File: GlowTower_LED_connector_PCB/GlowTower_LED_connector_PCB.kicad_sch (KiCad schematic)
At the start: 4 parts, among them U1 LED strip, U2 LED strip, U3 LED strip, U4 LED strip

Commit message: updated pcb design (in progress)
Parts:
- removed U1, U2, U3, U4: LED strip, Connector:LED strip connector pad, symbol Connector:LED_strip_contact_pads
- added SW1: TS-1102S-C-A-B, TS-1102S-C-A-B:TS-1102S-C-A-B, symbol TS-1102S-C-A-B:TS-1102S-C-A-B
- added U1, U2, U3, U4: (no value), symbol myparts:LED_strip_contact_4pads
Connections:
- new net: U1.3 (GND), U3.2 (Data)
- new net: U2.3 (GND), U4.2 (Data)
- new net BUTTON: SW1.1, U1.1 (5V)
- new net GND: SW1.3, U1.2 (Data)
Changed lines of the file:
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@@
 (kicad_sch (version 20211123) (generator eeschema)
   (paper "A5")
-  (wire (pts (xy 90.17 62.23) (xy 118.11 62.23))
+  (wire (pts (xy 90.17 64.77) (xy 105.41 64.77))
     (stroke (width 0) (type default) (color 0 0 0 0))
   )
-  (wire (pts (xy 90.17 77.47) (xy 118.11 77.47))
+  (wire (pts (xy 105.41 78.74) (xy 105.41 80.01))
+    (stroke (width 0) (type default) (color 0 0 0 0))
+  )
+  (wire (pts (xy 90.17 59.69) (xy 95.25 59.69))
+    (stroke (width 0) (type default) (color 0 0 0 0))
+  )
+  (wire (pts (xy 33.02 102.87) (xy 38.1 102.87))
+    (stroke (width 0) (type default) (color 0 0 0 0))
+  )
+  (wire (pts (xy 90.17 62.23) (xy 95.25 62.23))
+    (stroke (width 0) (type default) (color 0 0 0 0))
+  )
+  (wire (pts (xy 34.29 113.03) (xy 38.1 113.03))
+    (stroke (width 0) (type default) (color 0 0 0 0))
+  )
+  (wire (pts (xy 105.41 63.5) (xy 120.65 63.5))
+    (stroke (width 0) (type default) (color 0 0 0 0))
+  )
+  (wire (pts (xy 105.41 80.01) (xy 90.17 80.01))
+    (stroke (width 0) (type default) (color 0 0 0 0))
+  )
+  (wire (pts (xy 105.41 64.77) (xy 105.41 63.5))
+    (stroke (width 0) (type default) (color 0 0 0 0))
+  )
+  (wire (pts (xy 105.41 78.74) (xy 120.65 78.74))
     (stroke (width 0) (type default) (color 0 0 0 0))
   )
@@
     (effects (font (size 3 3)) (justify left bottom))
   )
-  (symbol (lib_name "LED_strip_contact_pads_7") (lib_id "Connector:LED_strip_contact_pads") (at 121.92 80.01 0) (mirror x) (unit 1)
-    (in_bom yes) (on_board yes)
-    (property "Reference" "U4" (id 0) (at 127 76.2 0)
-      (effects (font (size 1.27 1.27)) (justify left))
+  (global_label "BUTTON" (shape input) (at 95.25 59.69 0) (fields_autoplaced)
+    (effects (font (size 1.27 1.27)) (justify left))
+    (property "Intersheet References" "${INTERSHEET_REFS}" (id 0) (at 104.8598 59.6106 0)
+      (effects (font (size 1.27 1.27)) (justify left) hide)
     )
-    (property "Value" "LED strip" (id 1) (at 127 78.74 0)
-      (effects (font (size 1.27 1.27)) (justify left))
+  )
+  (global_label "BUTTON" (shape input) (at 33.02 102.87 180) (fields_autoplaced)
+    (effects (font (size 1.27 1.27)) (justify right))
+    (property "Intersheet References" "${INTERSHEET_REFS}" (id 0) (at 23.4102 102.9494 0)
+      (effects (font (size 1.27 1.27)) (justify right) hide)
     )
-    (property "Footprint" "Connector:LED strip connector pad" (id 2) (at 121.92 80.01 0)
+  )
+  (symbol (lib_id "power:GND") (at 95.25 62.23 90) (unit 1)
+    (in_bom yes) (on_board yes) (fields_autoplaced)
+    (property "Reference" "#PWR0101" (id 0) (at 101.6 62.23 0)
       (effects (font (size 1.27 1.27)) hide)
     )
-    (property "Datasheet" "" (id 3) (at 121.92 80.01 0)
+    (property "Value" "GND" (id 1) (at 99.06 62.2301 90)
+      (effects (font (size 1.27 1.27)) (justify right))
+    )
+    (property "Footprint" "" (id 2) (at 95.25 62.23 0)
       (effects (font (size 1.27 1.27)) hide)
+    )
+    (property "Datasheet" "" (id 3) (at 95.25 62.23 0)
+      (effects (font (size 1.27 1.27)) hide)
+    )
+    (pin "1")
+  )
+  (symbol (lib_id "TS-1102S-C-A-B:TS-1102S-C-A-B") (at 25.4 107.95 0) (unit 1)
+    (in_bom yes) (on_board yes) (fields_autoplaced)
+    (property "Reference" "SW1" (id 0) (at 50.8 97.79 0))
+    (property "Value" "TS-1102S-C-A-B" (id 1) (at 50.8 100.33 0))
+    (property "Footprint" "TS-1102S-C-A-B:TS-1102S-C-A-B" (id 2) (at 25.4 118.11 0)
+      (effects (font (size 1.27 1.27) italic) hide)
+    )
+    (property "Datasheet" "https://datasheet.lcsc.com/lcsc/2110151630_XKB-Connectivity-TS-1102S-C-A-B_C381038.pdf" (id 3) (at 23.114 107.823 0)
+      (effects (font (size 1.27 1.27)) (justify left) hide)
     )
     (pin "1")
     (pin "2")
     (pin "3")
+    (pin "4")
   )
-  (symbol (lib_name "LED_strip_contact_pads_6") (lib_id "Connector:LED_strip_contact_pads") (at 121.92 64.77 0) (mirror x) (unit 1)
+  (symbol (lib_id "myparts:LED_strip_contact_4pads") (at 86.36 59.69 0) (mirror y) (unit 1)
     (in_bom yes) (on_board yes)
-    (property "Reference" "U3" (id 0) (at 127 60.96 0)
+    (property "Reference" "U1" (id 0) (at 77.47 60.96 0)
       (effects (font (size 1.27 1.27)) (justify left))
     )
-    (property "Value" "LED strip" (id 1) (at 127 63.5 0)
+    (property "Value" "" (id 1) (at 77.47 63.5 0)
       (effects (font (size 1.27 1.27)) (justify left))
     )
-    (property "Footprint" "Connector:LED strip connector pad" (id 2) (at 121.92 64.77 0)
-      (effects (font (size 1.27 1.27)) hide)
-    )
-    (property "Datasheet" "" (id 3) (at 121.92 64.77 0)
-      (effects (font (size 1.27 1.27)) hide)
-    )
-    (pin "1")
-    (pin "2")
-    (pin "3")
-  )
-  (symbol (lib_name "LED_strip_contact_pads_3") (lib_id "Connector:LED_strip_contact_pads") (at 86.36 59.69 0) (mirror y) (unit 1)
-    (in_bom yes) (on_board yes)
-    (property "Reference" "U1" (id 0) (at 81.28 60.96 0)
-      (effects (font (size 1.27 1.27)) (justify left))
-    )
-    (property "Value" "LED strip" (id 1) (at 81.28 63.5 0)
-      (effects (font (size 1.27 1.27)) (justify left))
-    )
-    (property "Footprint" "Connector:LED strip connector pad" (id 2) (at 86.36 59.69 0)
+    (property "Footprint" "" (id 2) (at 86.36 59.69 0)
       (effects (font (size 1.27 1.27)) hide)
     )
@@
     (pin "2")
     (pin "3")
+    (pin "4")
   )
-  (symbol (lib_id "Connector:LED_strip_contact_pads") (at 86.36 74.93 0) (mirror y) (unit 1)
+  (symbol (lib_id "myparts:LED_strip_contact_4pads") (at 124.46 66.04 0) (mirror x) (unit 1)
     (in_bom yes) (on_board yes)
-    (property "Reference" "U2" (id 0) (at 78.74 74.93 0))
-    (property "Value" "LED strip" (id 1) (at 76.2 77.47 0))
-    (property "Footprint" "Connector:LED strip connector pad" (id 2) (at 86.36 74.93 0)
+    (property "Reference" "U3" (id 0) (at 134.62 60.96 0))
+    (property "Value" "" (id 1) (at 137.16 63.5 0))
+    (property "Footprint" "" (id 2) (at 124.46 66.04 0)
+      (effects (font (size 1.27 1.27)) hide)
+    )
+    (property "Datasheet" "" (id 3) (at 124.46 66.04 0)
+      (effects (font (size 1.27 1.27)) hide)
+    )
+    (pin "1")
+    (pin "2")
+    (pin "3")
+    (pin "4")
+  )
+  (symbol (lib_id "myparts:LED_strip_contact_4pads") (at 86.36 74.93 0) (mirror y) (unit 1)
+    (in_bom yes) (on_board yes)
+    (property "Reference" "U2" (id 0) (at 73.66 76.2 0))
+    (property "Value" "" (id 1) (at 73.66 78.74 0))
+    (property "Footprint" "" (id 2) (at 86.36 74.93 0)
       (effects (font (size 1.27 1.27)) hide)
     )
@@
     (pin "2")
     (pin "3")
+    (pin "4")
+  )
+  (symbol (lib_id "myparts:LED_strip_contact_4pads") (at 124.46 81.28 0) (mirror x) (unit 1)
+    (in_bom yes) (on_board yes)
+    (property "Reference" "U4" (id 0) (at 134.62 76.2 0))
+    (property "Value" "" (id 1) (at 137.16 78.74 0))
+    (property "Footprint" "" (id 2) (at 124.46 81.28 0)
+      (effects (font (size 1.27 1.27)) hide)
+    )
+    (property "Datasheet" "" (id 3) (at 124.46 81.28 0)
+      (effects (font (size 1.27 1.27)) hide)
+    )
+    (pin "1")
+    (pin "2")
+    (pin "3")
+    (pin "4")
+  )
+  (symbol (lib_id "power:GND") (at 34.29 113.03 270) (unit 1)
+    (in_bom yes) (on_board yes) (fields_autoplaced)
+    (property "Reference" "#PWR0102" (id 0) (at 27.94 113.03 0)
+      (effects (font (size 1.27 1.27)) hide)
+    )
+    (property "Value" "GND" (id 1) (at 30.48 113.0299 90)
+      (effects (font (size 1.27 1.27)) (justify right))
+    )
+    (property "Footprint" "" (id 2) (at 34.29 113.03 0)
+      (effects (font (size 1.27 1.27)) hide)
+    )
+    (property "Datasheet" "" (id 3) (at 34.29 113.03 0)
+      (effects (font (size 1.27 1.27)) hide)
+    )
+    (pin "1")
   )
   (sheet_instances
@@
   )
   (symbol_instances
-    (path "/ec5c2062-3a41-4636-8803-069e60a1641a"
-      (reference "U1") (unit 1) (value "LED strip") (footprint "Connector:LED strip connector pad")
+    (path "/21ef1968-a0fb-4b57-9c15-bd9b4521a1f0"
+      (reference "#PWR0101") (unit 1) (value "GND") (footprint "")
     )
-    (path "/f7667b23-296e-4362-a7e3-949632c8954b"
-      (reference "U2") (unit 1) (value "LED strip") (footprint "Connector:LED strip connector pad")
+    (path "/f102ecb1-5700-4820-807d-48fca6baaf4c"
+      (reference "#PWR0102") (unit 1) (value "GND") (footprint "")
     )
-    (path "/e4aa537c-eb9d-4dbb-ac87-fae46af42391"
-      (reference "U3") (unit 1) (value "LED strip") (footprint "Connector:LED strip connector pad")
+    (path "/3b3e6374-7870-4e9c-84dd-c6c9c8713fb1"
+      (reference "SW1") (unit 1) (value "TS-1102S-C-A-B") (footprint "TS-1102S-C-A-B:TS-1102S-C-A-B")
     )
-    (path "/9cbf35b8-f4d3-42a3-bb16-04ffd03fd8fd"
-      (reference "U4") (unit 1) (value "LED strip") (footprint "Connector:LED strip connector pad")
+    (path "/903d73dd-fd56-4103-90bf-a45d09a814bc"
+      (reference "U1") (unit 1) (value "LED strip") (footprint "myparts:LED strip connector 4pad supersmall")
+    )
+    (path "/b7b0b493-76e8-42d7-8e67-da2911f556ce"
+      (reference "U2") (unit 1) (value "LED strip") (footprint "myparts:LED strip connector 4pad supersmall")
+    )
+    (path "/a348a15e-9dd1-4384-9b04-af86a24d97fb"
+      (reference "U3") (unit 1) (value "LED strip") (footprint "myparts:LED strip connector 4pad supersmall")
+    )
+    (path "/d7a66b26-e013-45ce-92d1-9a5f78ecf5ef"
+      (reference "U4") (unit 1) (value "LED strip") (footprint "myparts:LED strip connector 4pad supersmall")
     )
   )

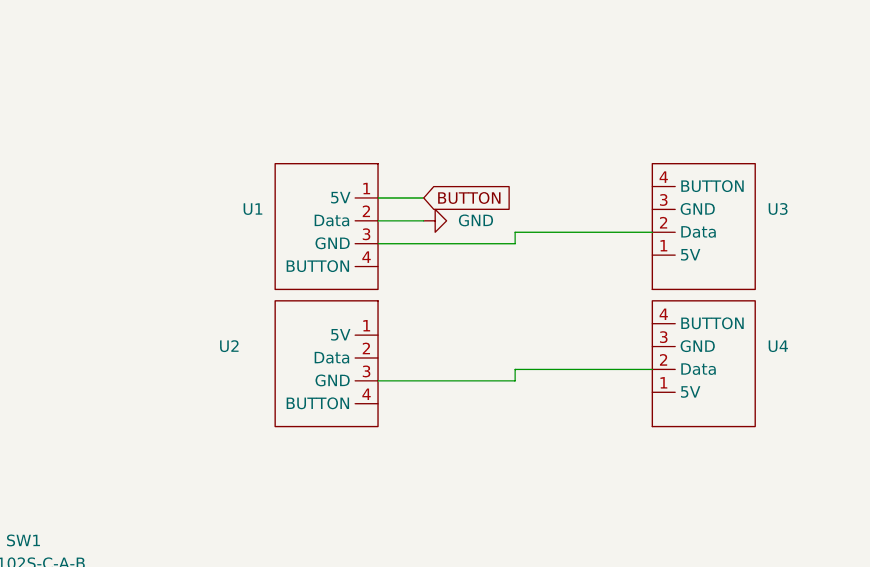
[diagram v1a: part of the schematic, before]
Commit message: redesigned GlowTower/GlowLight main pcb
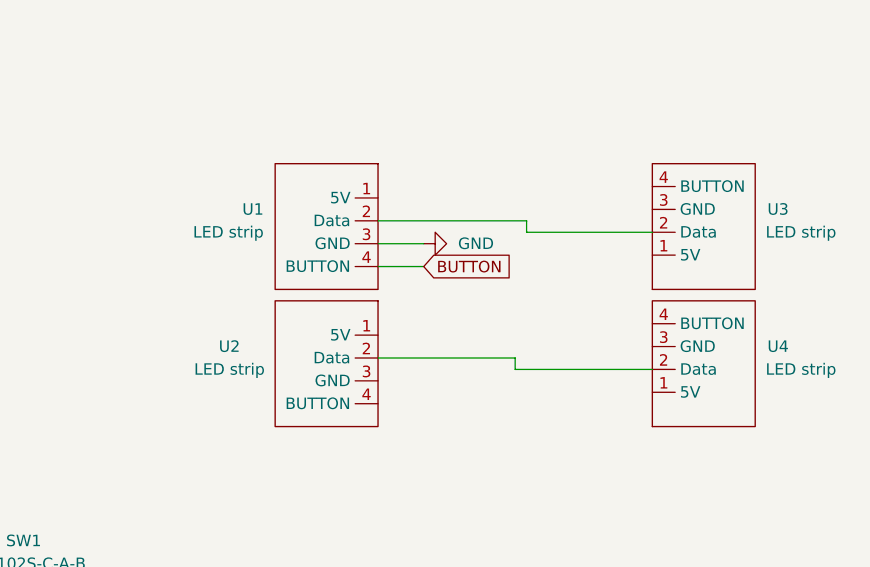
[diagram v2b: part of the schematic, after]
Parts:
- U1, U2, U3, U4: value (none) -> LED strip; footprint (none) -> myparts:LED strip connector 4pad
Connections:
- net BUTTON: now also U1.4 (BUTTON); no longer U1.1 (5V)
- net GND: now also U1.3 (GND); no longer U1.2 (Data)
- net at U3.2 (Data): now also U1.2 (Data); no longer U1.3 (GND)
- net at U2.2 (Data): now also U4.2 (Data)
- net at U2.3 (GND): no longer U4.2 (Data)
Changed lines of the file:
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@@
 (kicad_sch (version 20211123) (generator eeschema)
   (paper "A5")
-  (wire (pts (xy 90.17 64.77) (xy 105.41 64.77))
+  (wire (pts (xy 105.41 78.74) (xy 105.41 77.47))
     (stroke (width 0) (type default) (color 0 0 0 0))
   )
-  (wire (pts (xy 105.41 78.74) (xy 105.41 80.01))
+  (wire (pts (xy 90.17 62.23) (xy 106.68 62.23))
     (stroke (width 0) (type default) (color 0 0 0 0))
   )
-  (wire (pts (xy 90.17 59.69) (xy 95.25 59.69))
+  (wire (pts (xy 106.68 63.5) (xy 120.65 63.5))
     (stroke (width 0) (type default) (color 0 0 0 0))
   )
@@
     (stroke (width 0) (type default) (color 0 0 0 0))
   )
-  (wire (pts (xy 90.17 62.23) (xy 95.25 62.23))
+  (wire (pts (xy 90.17 67.31) (xy 95.25 67.31))
     (stroke (width 0) (type default) (color 0 0 0 0))
   )
@@
     (stroke (width 0) (type default) (color 0 0 0 0))
   )
-  (wire (pts (xy 105.41 63.5) (xy 120.65 63.5))
+  (wire (pts (xy 90.17 64.77) (xy 95.25 64.77))
     (stroke (width 0) (type default) (color 0 0 0 0))
   )
-  (wire (pts (xy 105.41 80.01) (xy 90.17 80.01))
+  (wire (pts (xy 90.17 77.47) (xy 105.41 77.47))
     (stroke (width 0) (type default) (color 0 0 0 0))
   )
-  (wire (pts (xy 105.41 64.77) (xy 105.41 63.5))
+  (wire (pts (xy 106.68 62.23) (xy 106.68 63.5))
     (stroke (width 0) (type default) (color 0 0 0 0))
   )
@@
     (effects (font (size 3 3)) (justify left bottom))
   )
-  (global_label "BUTTON" (shape input) (at 95.25 59.69 0) (fields_autoplaced)
+  (global_label "BUTTON" (shape input) (at 95.25 67.31 0) (fields_autoplaced)
     (effects (font (size 1.27 1.27)) (justify left))
-    (property "Intersheet References" "${INTERSHEET_REFS}" (id 0) (at 104.8598 59.6106 0)
+    (property "Intersheet References" "${INTERSHEET_REFS}" (id 0) (at 104.8598 67.2306 0)
       (effects (font (size 1.27 1.27)) (justify left) hide)
     )
@@
     )
   )
-  (symbol (lib_id "power:GND") (at 95.25 62.23 90) (unit 1)
+  (symbol (lib_id "power:GND") (at 95.25 64.77 90) (unit 1)
     (in_bom yes) (on_board yes) (fields_autoplaced)
-    (property "Reference" "#PWR0101" (id 0) (at 101.6 62.23 0)
+    (property "Reference" "#PWR0101" (id 0) (at 101.6 64.77 0)
       (effects (font (size 1.27 1.27)) hide)
     )
-    (property "Value" "GND" (id 1) (at 99.06 62.2301 90)
+    (property "Value" "GND" (id 1) (at 99.06 64.7701 90)
       (effects (font (size 1.27 1.27)) (justify right))
     )
-    (property "Footprint" "" (id 2) (at 95.25 62.23 0)
+    (property "Footprint" "" (id 2) (at 95.25 64.77 0)
       (effects (font (size 1.27 1.27)) hide)
     )
-    (property "Datasheet" "" (id 3) (at 95.25 62.23 0)
+    (property "Datasheet" "" (id 3) (at 95.25 64.77 0)
       (effects (font (size 1.27 1.27)) hide)
     )
@@
       (effects (font (size 1.27 1.27)) (justify left))
     )
-    (property "Value" "" (id 1) (at 77.47 63.5 0)
+    (property "Value" "LED strip" (id 1) (at 77.47 63.5 0)
       (effects (font (size 1.27 1.27)) (justify left))
     )
-    (property "Footprint" "" (id 2) (at 86.36 59.69 0)
+    (property "Footprint" "myparts:LED strip connector 4pad" (id 2) (at 86.36 59.69 0)
       (effects (font (size 1.27 1.27)) hide)
     )
@@
     (in_bom yes) (on_board yes)
     (property "Reference" "U3" (id 0) (at 134.62 60.96 0))
-    (property "Value" "" (id 1) (at 137.16 63.5 0))
-    (property "Footprint" "" (id 2) (at 124.46 66.04 0)
+    (property "Value" "LED strip" (id 1) (at 137.16 63.5 0))
+    (property "Footprint" "myparts:LED strip connector 4pad" (id 2) (at 124.46 66.04 0)
       (effects (font (size 1.27 1.27)) hide)
     )
@@
     (in_bom yes) (on_board yes)
     (property "Reference" "U2" (id 0) (at 73.66 76.2 0))
-    (property "Value" "" (id 1) (at 73.66 78.74 0))
-    (property "Footprint" "" (id 2) (at 86.36 74.93 0)
+    (property "Value" "LED strip" (id 1) (at 73.66 78.74 0))
+    (property "Footprint" "myparts:LED strip connector 4pad" (id 2) (at 86.36 74.93 0)
       (effects (font (size 1.27 1.27)) hide)
     )
@@
     (in_bom yes) (on_board yes)
     (property "Reference" "U4" (id 0) (at 134.62 76.2 0))
-    (property "Value" "" (id 1) (at 137.16 78.74 0))
-    (property "Footprint" "" (id 2) (at 124.46 81.28 0)
+    (property "Value" "LED strip" (id 1) (at 137.16 78.74 0))
+    (property "Footprint" "myparts:LED strip connector 4pad" (id 2) (at 124.46 81.28 0)
       (effects (font (size 1.27 1.27)) hide)
     )
@@
     )
     (path "/903d73dd-fd56-4103-90bf-a45d09a814bc"
-      (reference "U1") (unit 1) (value "LED strip") (footprint "myparts:LED strip connector 4pad supersmall")
+      (reference "U1") (unit 1) (value "LED strip") (footprint "myparts:LED strip connector 4pad")
     )
     (path "/b7b0b493-76e8-42d7-8e67-da2911f556ce"
-      (reference "U2") (unit 1) (value "LED strip") (footprint "myparts:LED strip connector 4pad supersmall")
+      (reference "U2") (unit 1) (value "LED strip") (footprint "myparts:LED strip connector 4pad")
     )
     (path "/a348a15e-9dd1-4384-9b04-af86a24d97fb"
-      (reference "U3") (unit 1) (value "LED strip") (footprint "myparts:LED strip connector 4pad supersmall")
+      (reference "U3") (unit 1) (value "LED strip") (footprint "myparts:LED strip connector 4pad")
     )
     (path "/d7a66b26-e013-45ce-92d1-9a5f78ecf5ef"
-      (reference "U4") (unit 1) (value "LED strip") (footprint "myparts:LED strip connector 4pad supersmall")
+      (reference "U4") (unit 1) (value "LED strip") (footprint "myparts:LED strip connector 4pad")
     )
   )

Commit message: added release candidate 1 update
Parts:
- removed SW1: TS-1102S-C-A-B, TS-1102S-C-A-B:TS-1102S-C-A-B, symbol TS-1102S-C-A-B:TS-1102S-C-A-B
- removed U1, U2, U3, U4: LED strip, myparts:LED strip connector 4pad, symbol myparts:LED_strip_contact_4pads
- added SW1: TS-1102S-C-A-B, footprint:KEY-SMD_4P-L6.0-W6.0-P4.50-LS8.6, symbol MyParts:TS-1102S-C-A-B
- added U1, U2, U3, U4: (no value), symbol MyParts:LED_strip_contact_4pads
- added U5, U6: SMTSO3015CTJ, footprint:SMTSO3030CTJ, symbol MyParts:SMTSO3015CTJ
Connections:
- net BUTTON: now also SW1.1, U1.4 (BUTTON)
- net GND: now also SW1.3, U1.3 (GND)
- new net: U1.2 (Data), U3.2 (Data)
- new net: U2.2 (Data), U4.2 (Data)
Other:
- note added: "Button"
- note added: "Connector Pads"
- note added: "Nuts"
- note removed: "LED strip connector PCB"

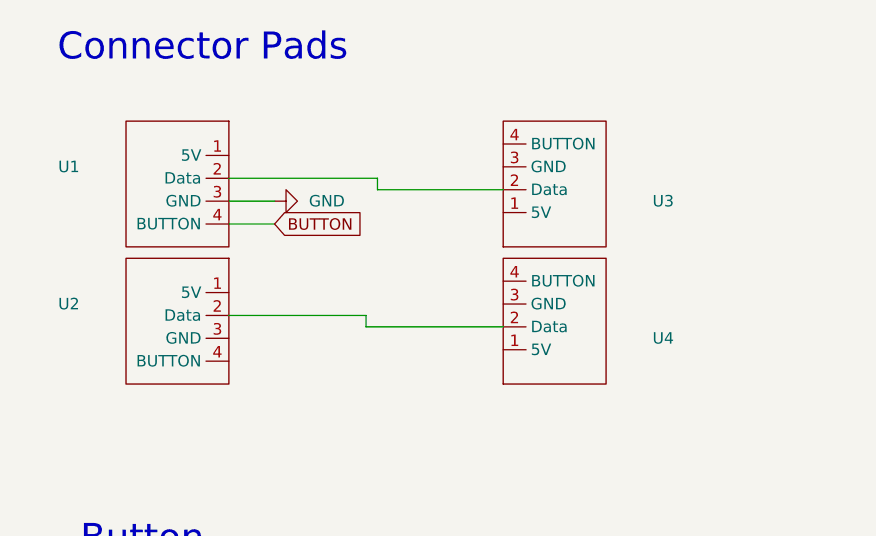
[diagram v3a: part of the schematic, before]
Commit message: fixed capacitor value
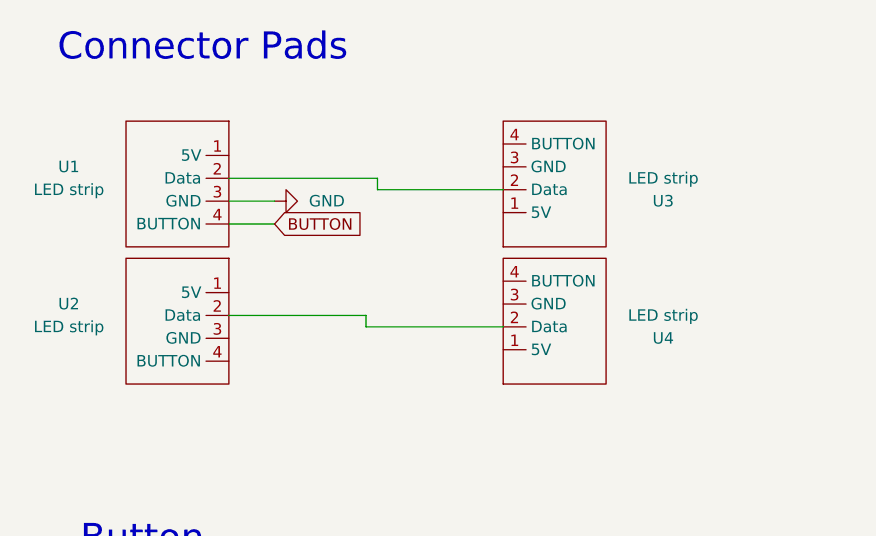
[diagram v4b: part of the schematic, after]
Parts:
- U1, U2, U3, U4: value (none) -> LED strip; footprint (none) -> footprint:LED strip connector 4pad
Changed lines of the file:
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@@
     (in_bom no) (on_board yes)
     (property "Reference" "U3" (id 0) (at 85.09 36.83 0))
-    (property "Value" "" (id 1) (at 85.09 34.29 0))
-    (property "Footprint" "" (id 2) (at 71.12 38.1 0)
+    (property "Value" "LED strip" (id 1) (at 85.09 34.29 0))
+    (property "Footprint" "footprint:LED strip connector 4pad" (id 2) (at 71.12 38.1 0)
       (effects (font (size 1.27 1.27)) hide)
     )
@@
     (in_bom no) (on_board yes)
     (property "Reference" "U1" (id 0) (at 19.05 33.02 0))
-    (property "Value" "" (id 1) (at 19.05 35.56 0))
-    (property "Footprint" "" (id 2) (at 33.02 31.75 0)
+    (property "Value" "LED strip" (id 1) (at 19.05 35.56 0))
+    (property "Footprint" "footprint:LED strip connector 4pad" (id 2) (at 33.02 31.75 0)
       (effects (font (size 1.27 1.27)) hide)
     )
@@
     (in_bom no) (on_board yes)
     (property "Reference" "U2" (id 0) (at 19.05 48.26 0))
-    (property "Value" "" (id 1) (at 19.05 50.8 0))
-    (property "Footprint" "" (id 2) (at 33.02 46.99 0)
+    (property "Value" "LED strip" (id 1) (at 19.05 50.8 0))
+    (property "Footprint" "footprint:LED strip connector 4pad" (id 2) (at 33.02 46.99 0)
       (effects (font (size 1.27 1.27)) hide)
     )
@@
     (in_bom no) (on_board yes)
     (property "Reference" "U4" (id 0) (at 85.09 52.07 0))
-    (property "Value" "" (id 1) (at 85.09 49.53 0))
-    (property "Footprint" "" (id 2) (at 71.12 53.34 0)
+    (property "Value" "LED strip" (id 1) (at 85.09 49.53 0))
+    (property "Footprint" "footprint:LED strip connector 4pad" (id 2) (at 71.12 53.34 0)
       (effects (font (size 1.27 1.27)) hide)
     )
